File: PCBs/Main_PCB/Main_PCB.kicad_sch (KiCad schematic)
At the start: 12 parts, among them J1 Light_Header, J2 OLED_Header, J3 Button_PCB_Header, J4 USB_A, J5 USB_A, Q1 2N3904, Q2 2N3904, U1 Pico, U2 DS1302+, Y1 Crystal

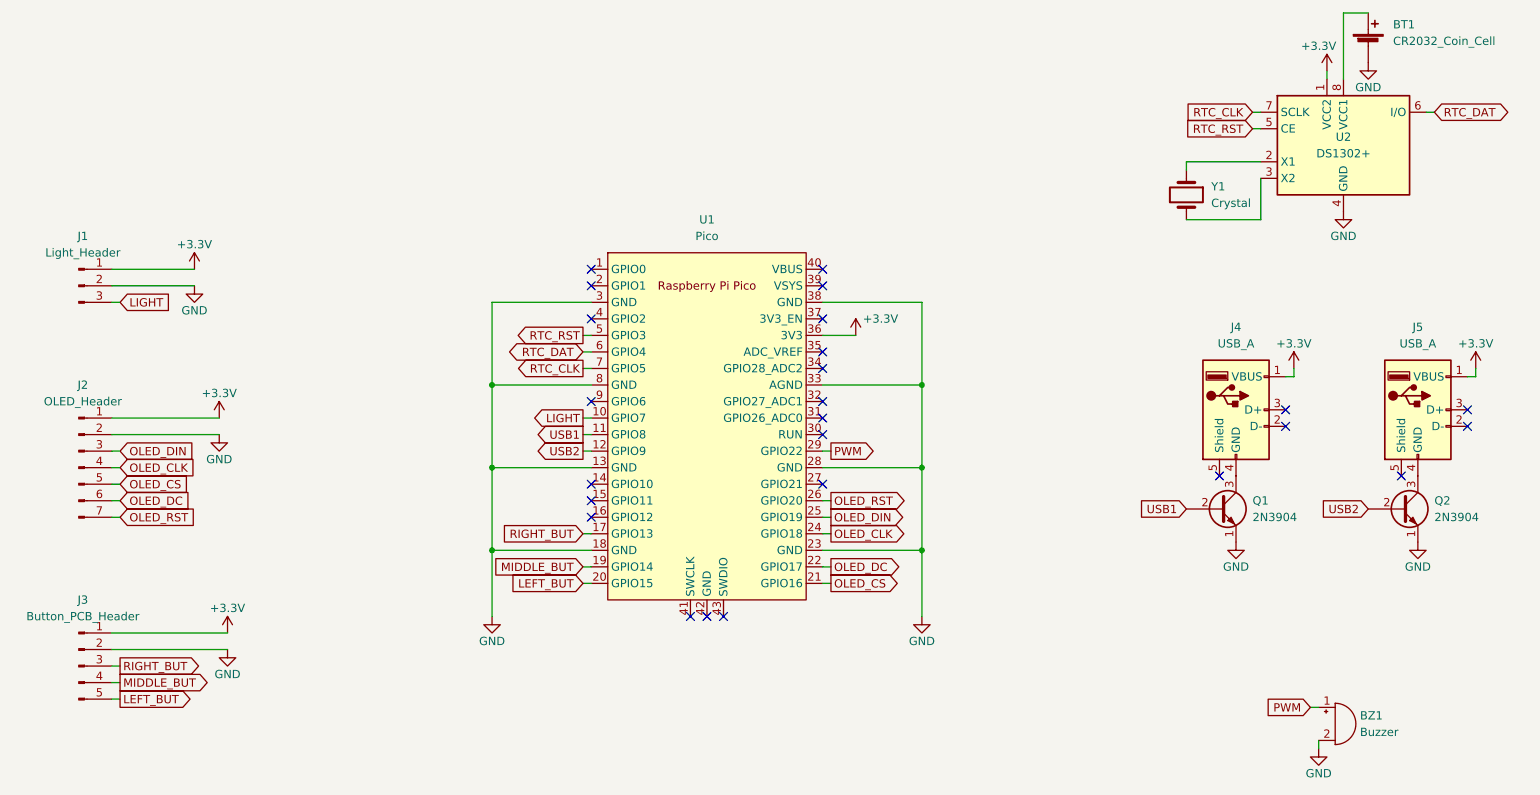
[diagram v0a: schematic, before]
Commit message: V3.2.0-alpha Designed Main PCB
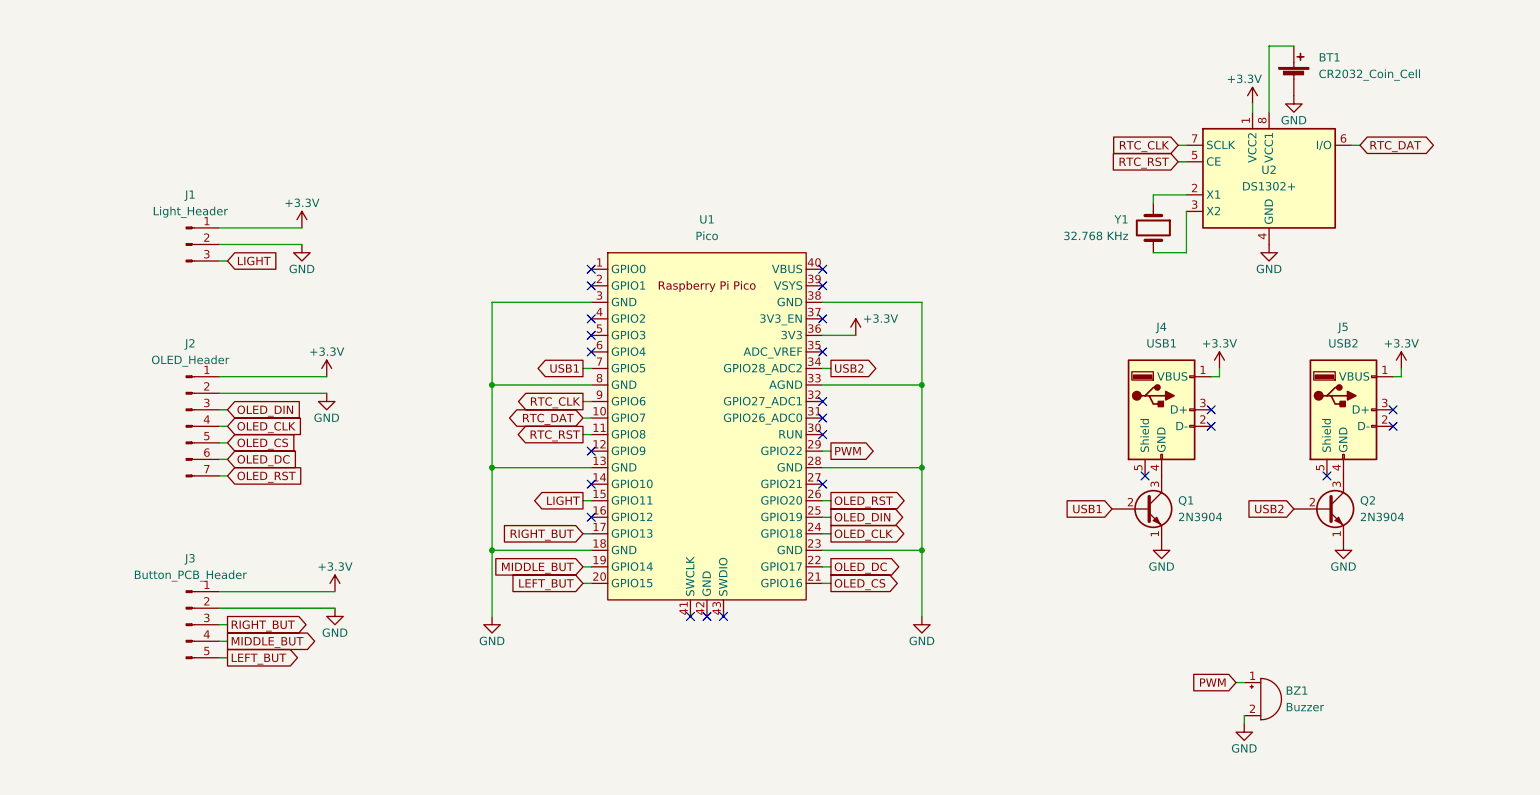
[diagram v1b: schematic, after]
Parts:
- BT1: footprint (none) -> Vertical_CR2032_Battery_Holder:Vertical_CR2032_Battery_Holder
- BZ1: footprint (none) -> Buzzer_Beeper:Buzzer_12x9.5RM7.6
- J1: footprint (none) -> Connector_PinHeader_2.54mm:PinHeader_1x03_P2.54mm_Vertical
- J2: footprint (none) -> Connector_PinHeader_2.54mm:PinHeader_1x07_P2.54mm_Vertical
- J3: footprint (none) -> Connector_PinHeader_2.54mm:PinHeader_1x05_P2.54mm_Vertical
- J4: value USB_A -> USB1; footprint (none) -> Connector_USB:USB_A_CONNFLY_DS1095-WNR0
- J5: value USB_A -> USB2; footprint (none) -> Connector_USB:USB_A_CONNFLY_DS1095-WNR0
- U1: footprint RPi_Pico:RPi_Pico_SMD_TH -> MCU_RaspberryPi_and_Boards:RPi_Pico_SMD_TH
- Y1: value Crystal -> 32.768 KHz; footprint (none) -> Crystal:Crystal_DS26_D2.0mm_L6.0mm_Horizontal
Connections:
- net LIGHT: now also U1.15 (GPIO11); no longer U1.10 (GPIO7)
- net RTC_CLK: now also U1.9 (GPIO6); no longer U1.7 (GPIO5)
- net RTC_DAT: now also U1.10 (GPIO7); no longer U1.6 (GPIO4)
- net RTC_RST: now also U1.11 (GPIO8); no longer U1.5 (GPIO3)
- net USB1: now also U1.7 (GPIO5); no longer U1.11 (GPIO8)
- net USB2: now also U1.34 (GPIO28_ADC2); no longer U1.12 (GPIO9)
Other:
- moved on the sheet: BT1, BZ1, J1, J2, J3, J4, J5, Q1, Q2, U2, Y1

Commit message: V3.4.2-alpha Changed Buzzer Footprint
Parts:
- BZ1: footprint Buzzer_Beeper:Buzzer_12x9.5RM7.6 -> Buzzer_Beeper:MagneticBuzzer_ProSignal_ABT-410-RC
- J1: value Light_Header -> LIGHT
- J2: value OLED_Header -> OLED
- J3: value Button_PCB_Header -> BUTTONS
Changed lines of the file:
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@@
       (effects (font (size 1.27 1.27)) (justify left))
     )
-    (property "Footprint" "Buzzer_Beeper:Buzzer_12x9.5RM7.6" (id 2) (at 240.665 123.19 90)
+    (property "Footprint" "Buzzer_Beeper:MagneticBuzzer_ProSignal_ABT-410-RC" (id 2) (at 240.665 123.19 90)
       (effects (font (size 1.27 1.27)) hide)
     )
@@
     (in_bom yes) (on_board yes) (fields_autoplaced)
     (property "Reference" "J3" (id 0) (at 76.835 104.14 0))
-    (property "Value" "Button_PCB_Header" (id 1) (at 76.835 106.68 0))
+    (property "Value" "BUTTONS" (id 1) (at 76.835 106.68 0))
     (property "Footprint" "Connector_PinHeader_2.54mm:PinHeader_1x05_P2.54mm_Vertical" (id 2) (at 76.2 114.3 0)
       (effects (font (size 1.27 1.27)) hide)
@@
     (in_bom yes) (on_board yes) (fields_autoplaced)
     (property "Reference" "J1" (id 0) (at 76.835 48.26 0))
-    (property "Value" "Light_Header" (id 1) (at 76.835 50.8 0))
+    (property "Value" "LIGHT" (id 1) (at 76.835 50.8 0))
     (property "Footprint" "Connector_PinHeader_2.54mm:PinHeader_1x03_P2.54mm_Vertical" (id 2) (at 76.2 55.88 0)
       (effects (font (size 1.27 1.27)) hide)
@@
     (in_bom yes) (on_board yes) (fields_autoplaced)
     (property "Reference" "J2" (id 0) (at 76.835 71.12 0))
-    (property "Value" "OLED_Header" (id 1) (at 76.835 73.66 0))
+    (property "Value" "OLED" (id 1) (at 76.835 73.66 0))
     (property "Footprint" "Connector_PinHeader_2.54mm:PinHeader_1x07_P2.54mm_Vertical" (id 2) (at 76.2 83.82 0)
       (effects (font (size 1.27 1.27)) hide)
@@
     )
     (path "/3143f425-d5f6-48ae-8658-98125daba029"
-      (reference "BZ1") (unit 1) (value "Buzzer") (footprint "Buzzer_Beeper:Buzzer_12x9.5RM7.6")
+      (reference "BZ1") (unit 1) (value "Buzzer") (footprint "Buzzer_Beeper:MagneticBuzzer_ProSignal_ABT-410-RC")
     )
     (path "/d6a0b0bd-596f-43a4-b39d-122e622be668"
-      (reference "J1") (unit 1) (value "Light_Header") (footprint "Connector_PinHeader_2.54mm:PinHeader_1x03_P2.54mm_Vertical")
+      (reference "J1") (unit 1) (value "LIGHT") (footprint "Connector_PinHeader_2.54mm:PinHeader_1x03_P2.54mm_Vertical")
     )
     (path "/e4e10fa2-50c8-4e17-ba3f-7a9e8e6d0651"
-      (reference "J2") (unit 1) (value "OLED_Header") (footprint "Connector_PinHeader_2.54mm:PinHeader_1x07_P2.54mm_Vertical")
+      (reference "J2") (unit 1) (value "OLED") (footprint "Connector_PinHeader_2.54mm:PinHeader_1x07_P2.54mm_Vertical")
     )
     (path "/3a61dbb5-a7fd-456c-9073-9446bd30be91"
-      (reference "J3") (unit 1) (value "Button_PCB_Header") (footprint "Connector_PinHeader_2.54mm:PinHeader_1x05_P2.54mm_Vertical")
+      (reference "J3") (unit 1) (value "BUTTONS") (footprint "Connector_PinHeader_2.54mm:PinHeader_1x05_P2.54mm_Vertical")
     )
     (path "/849b0b92-5dbf-44f9-924d-0c71b58eb15a"
